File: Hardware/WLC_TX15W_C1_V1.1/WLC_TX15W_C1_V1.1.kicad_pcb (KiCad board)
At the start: 2 copper layers, 57.3 x 42.3 mm, 129 parts, among them J1 Conn_01x05, J2 PWR, Q1 BSZ0910LS, Q2 BSZ0910LS, Q3 BSZ0910LS, Q4 BSS138, Q5 BSZ0910LS, Q6 BSZ0910LS, Q7 BSZ0910LS, Q8 BSS138, Q9 AO3400A, U2 LM358, U3 SLS32AIA020X2USON10XTMA4, U4 WLC1115-68LQXQ, Y2 SG-210STF

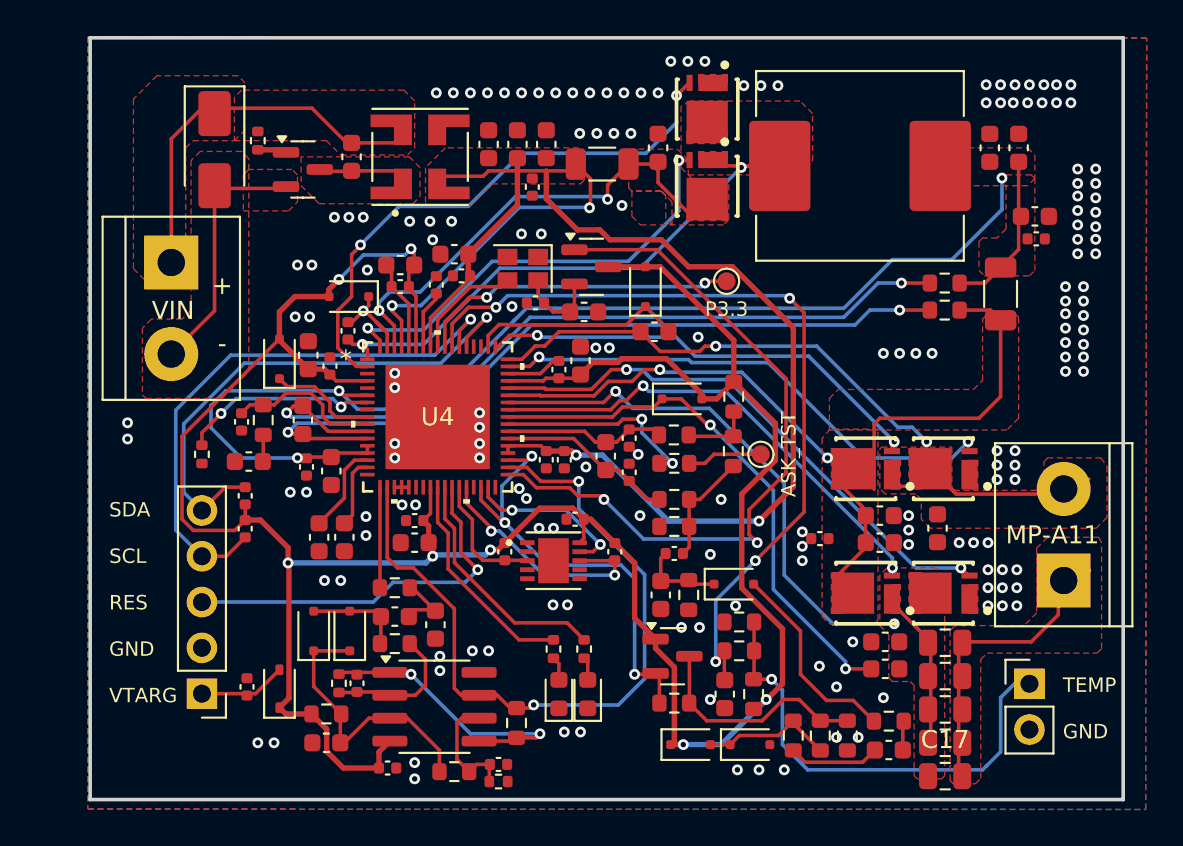
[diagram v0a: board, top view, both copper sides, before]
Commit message: add usb type c
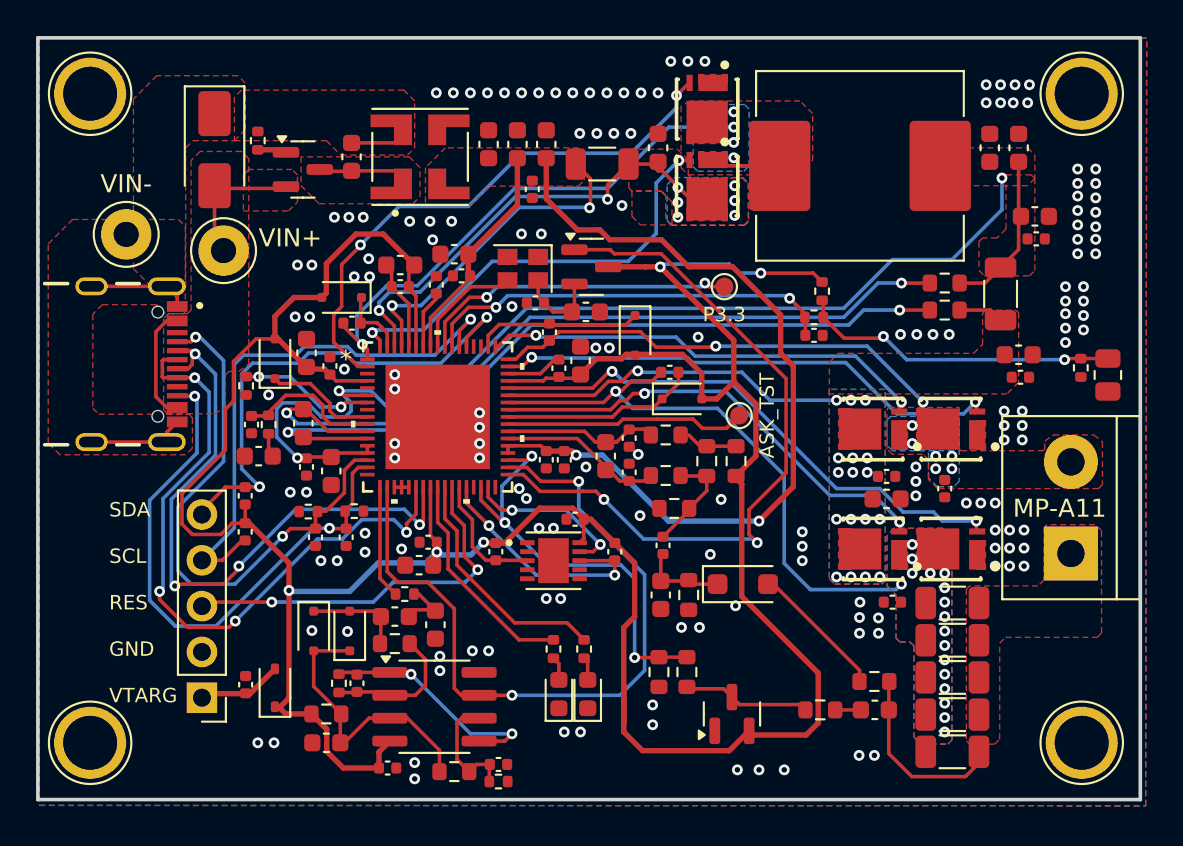
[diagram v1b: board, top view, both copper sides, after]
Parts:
- removed D12, D13: BAT54J, Diode_SMD:D_SOD-323F
- removed J2: PWR, TerminalBlock:TerminalBlock_bornier-2_P5.08mm
- removed Q4: BSS138, Package_TO_SOT_SMD:SOT-23
- removed R33: 0R, Resistor_SMD:R_0603_1608Metric
- added C61: 0.1uF, Capacitor_SMD:C_0402_1005Metric, F.Cu at (156.6, 68.7)
- added D15: MMBD1503, Package_TO_SOT_SMD:SOT-23, F.Cu at (140.6, 87.4)
- added J3: USB4105-GF-A, Footprints-Models:GCT_USB4105-GF-A, F.Cu at (105.1, 68.0)
- added TP3: VIN+, TestPoint:TestPoint_Loop_D3.50mm_Drill1.4mm_Beaded, F.Cu at (112.4, 61.7)
- added TP4: VIN-, TestPoint:TestPoint_Loop_D3.50mm_Drill1.4mm_Beaded, F.Cu at (107.0, 60.8)
- added TP5: GND, TestPoint:TestPoint_Plated_Hole_D3.0mm, F.Cu at (160.0, 53.0)
- added TP6: GND, TestPoint:TestPoint_Plated_Hole_D3.0mm, F.Cu at (105.0, 53.0)
- added TP7: GND, TestPoint:TestPoint_Plated_Hole_D3.0mm, F.Cu at (160.0, 89.0)
- added TP8: GND, TestPoint:TestPoint_Plated_Hole_D3.0mm, F.Cu at (105.0, 89.0)
- C16, C17, C18, C19, C20: footprint Capacitor_SMD:C_0805_2012Metric -> Capacitor_SMD:C_1206_3216Metric
- C2, C23, C24, C25, C26, C31, C32: footprint Capacitor_SMD:C_0603_1608Metric -> Capacitor_SMD:C_0402_1005Metric
- C6: value 100pF -> 150pF
- D10, D4, D5, D6, D7, D9: value BAT54J -> 1PS76SB21
- D11: value BAT54J -> BAS16H; footprint Diode_SMD:D_SOD-323F -> Diode_SMD:D_SOD-123F
- R18, R3, R4, R6, TH1: footprint Resistor_SMD:R_0603_1608Metric -> Resistor_SMD:R_0402_1005Metric
- R22: value 0R -> 5.1K; footprint Resistor_SMD:R_0603_1608Metric -> Resistor_SMD:R_0402_1005Metric
- R9: value 1M -> 5.1K; footprint Resistor_SMD:R_0603_1608Metric -> Resistor_SMD:R_0402_1005Metric
- TH2: footprint Connector_PinHeader_2.54mm:PinHeader_1x02_P2.54mm_Vertical -> Resistor_SMD:R_0805_2012Metric
- moved TH1 23.6 mm to (159.9, 68.2), turned to -90 degrees
- moved R3 22.7 mm to (145.6, 64.0), turned to 90 degrees
- moved C2 20.5 mm to (145.2, 66.4), turned to 180 degrees
- moved R22 20.5 mm to (117.1, 76.2), turned to 0 degrees
- moved C25 20.3 mm to (137.2, 68.5), turned to 0 degrees
- moved R4 19.0 mm to (145.2, 65.4)
- moved TH2 17.7 mm to (161.4, 68.6), turned to -90 degrees
- moved R9 14.8 mm to (119.7, 76.2), turned to 180 degrees
- moved C22 11.8 mm to (156.5, 67.5)
- moved R32 11.0 mm to (136.6, 85.1)
- moved R31 8.20 mm to (138.1, 85.1)
- moved C26 5.83 mm to (130.5, 66.2), turned to 90 degrees
- moved C60 5.06 mm to (149.2, 74.2), turned to 180 degrees
- moved R21 4.52 mm to (113.7, 69.2)
- moved R25 3.58 mm to (140.8, 73.4), turned to 90 degrees
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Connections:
- net CSNO_0 renamed /CSNO_0
- net CSPO_0 renamed /CSPO_0
- net Net-(D8-A1) renamed USB-GND
- net Net-(D8-A2) renamed USB-IN
- C3 pad 2: Net-(D4-K) -> Net-(D4-A)
- C5 pad 1: Net-(D4-A) -> Net-(D4-K)
- D5 pad 1: Net-(D4-K) -> Net-(D4-A)
- D5 pad 2: Net-(D4-A) -> Net-(D4-K)
- R11 pad 2: Net-(D4-K) -> Net-(D4-A)
- R22 pad 1: ASK_TST -> GND
- R22 pad 2: Net-(U4-ASK_TST) -> CC1_0
- R31 pad 2: Net-(Q4-D) -> Q_COMP
- R32 pad 1: Net-(Q4-D) -> Q_COMP
- R5 pad 2: Net-(D4-K) -> Net-(D4-A)
- R7 pad 2: Net-(D4-A) -> Net-(D4-K)
- R9 pad 1: ASK_DEMOD -> GND
- R9 pad 2: Net-(U2B-+) -> CC2_0
- U2 pad 3: Net-(D4-K) -> Net-(D4-A)
- U4 pad 42: Net-(U4-ASK_TST) -> ASK_TST
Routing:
- net D+_0: track 0.00 -> 37.2 mm, vias 0 -> 4
- net D-_0: track 0.00 -> 35.4 mm, vias 0 -> 4
- net CC2_0: track 3.92 -> 31.4 mm, vias 0 -> 2
- net CC1_0: track 5.03 -> 30.5 mm, vias 0 -> 2
- net IOUT_CSN_0: track 44.8 -> 22.0 mm, vias 2 -> 18
- net TEMP_FB1: track 45.6 -> 23.1 mm, vias 4 -> 2
- net VDD: track 152.9 -> 172.4 mm, vias 7 -> 5
- net BST2_1: track 30.3 -> 10.8 mm, vias 2 -> 0
- net SW1_1: track 41.5 -> 25.8 mm, vias 2 -> 8
- net Net-(Q4-D): track 12.8 -> 0.00 mm
- net Net-(U4-ASK_TST): track 11.4 -> 0.00 mm, vias 2 -> 0
- net Net-(D4-K): track 15.7 -> 5.37 mm
- net Net-(D4-A): track 5.37 -> 15.7 mm
- net ASK_TST: track 4.19 -> 13.4 mm
- net Net-(R3-Pad1): track 26.1 -> 17.8 mm, vias 1 -> 2
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- added copper zone on B.Cu, net IIN_CSN_0
- added copper zone on B.Cu, net IOUT_CSN_0
- added copper zone on B.Cu, net SW1_0
- added copper zone on B.Cu, net SW1_1
- added copper zone on B.Cu, net SW2_1
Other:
- board size 57.3 x 42.3 mm -> 61.2 x 42.3 mm
- board text removed: "+ -"
- board text removed: "TEMP GND"
- board text removed: "VIN"

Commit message: update bom
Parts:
- removed TP1: P3.3, TestPoint:TestPoint_Pad_D1.0mm
- removed TP2: ASK_TST, TestPoint:TestPoint_Pad_D1.0mm
- added G***: LOGO, haidv-library:LoGo12mm, B.Cu at (115.6, 55.6)
- C2, C23, C24, C35, C50, C51: footprint Capacitor_SMD:C_0402_1005Metric -> Capacitor_SMD:C_0603_1608Metric
- C3, C33, C4, C5: footprint Capacitor_SMD:C_0603_1608Metric -> Capacitor_SMD:C_0402_1005Metric
- L1: footprint Inductor_SMD:L_Bourns_SRP1050WA -> Inductor_SMD:L_Bourns-SRN8040_8x8.15mm
- R14, R15, R16, R17: footprint Capacitor_SMD:C_0402_1005Metric -> Resistor_SMD:R_0402_1005Metric
- R19, R20, R23, R24, R27, R28, R29, R5, R7: footprint Resistor_SMD:R_0603_1608Metric -> Resistor_SMD:R_0402_1005Metric
- moved R29 6.89 mm to (143.9, 80.4), turned to -90 degrees
- moved D5 5.96 mm to (116.5, 88.0)
- moved C4 5.39 mm to (118.8, 83.4)
- moved D4 5.27 mm to (118.4, 88.0)
- moved R7 4.44 mm to (117.8, 85.3), turned to 90 degrees
- moved C5 4.29 mm to (117.8, 83.4), turned to 90 degrees
- moved C14 3.75 mm to (152.8, 56.0)
- moved C15 3.75 mm to (151.2, 56.0)
- moved R6 3.68 mm to (118.8, 81.5), turned to -90 degrees
- moved C58 3.24 mm to (154.2, 61.4)
- moved C57 3.12 mm to (154.3, 60.1)
- moved D15 2.75 mm to (140.6, 84.7), turned to -90 degrees
- moved D3 2.68 mm to (114.0, 88.3)
- moved C22 2.55 mm to (153.9, 67.5)
- moved C61 2.55 mm to (154.1, 68.8)
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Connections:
- U4 pad 42: ASK_TST -> unconnected-(U4-ASK_TST-Pad42)
- U4 pad 59: P3.3 -> unconnected-(U4-GPIO12-Pad59)
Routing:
- net P3.3: track 17.8 -> 0.00 mm, vias 2 -> 0
- net VDD: track 172.4 -> 154.7 mm
- net ASK_TST: track 13.4 -> 0.00 mm
- net IOUT_CSP_0: track 67.8 -> 58.1 mm
- net COIL_SNS: track 10.5 -> 17.3 mm
- net Net-(D11-A): track 7.68 -> 1.47 mm
- net CC1_0: track 30.5 -> 24.8 mm
- net Net-(D4-A): track 15.7 -> 11.0 mm
- net Net-(U2A--): track 7.79 -> 3.79 mm
- net IIN_CSP_0: track 79.5 -> 76.5 mm
- net Net-(D15-common): track 7.06 -> 5.20 mm
- net CTRL_1: track 40.2 -> 38.5 mm
- net /CSPO_0: track 44.2 -> 42.6 mm
- net /CSNO_0: track 43.0 -> 41.3 mm
- net ASK_DEMOD: track 41.2 -> 39.7 mm
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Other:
- board text added: "WLC_TX15W_C1_V1.1"

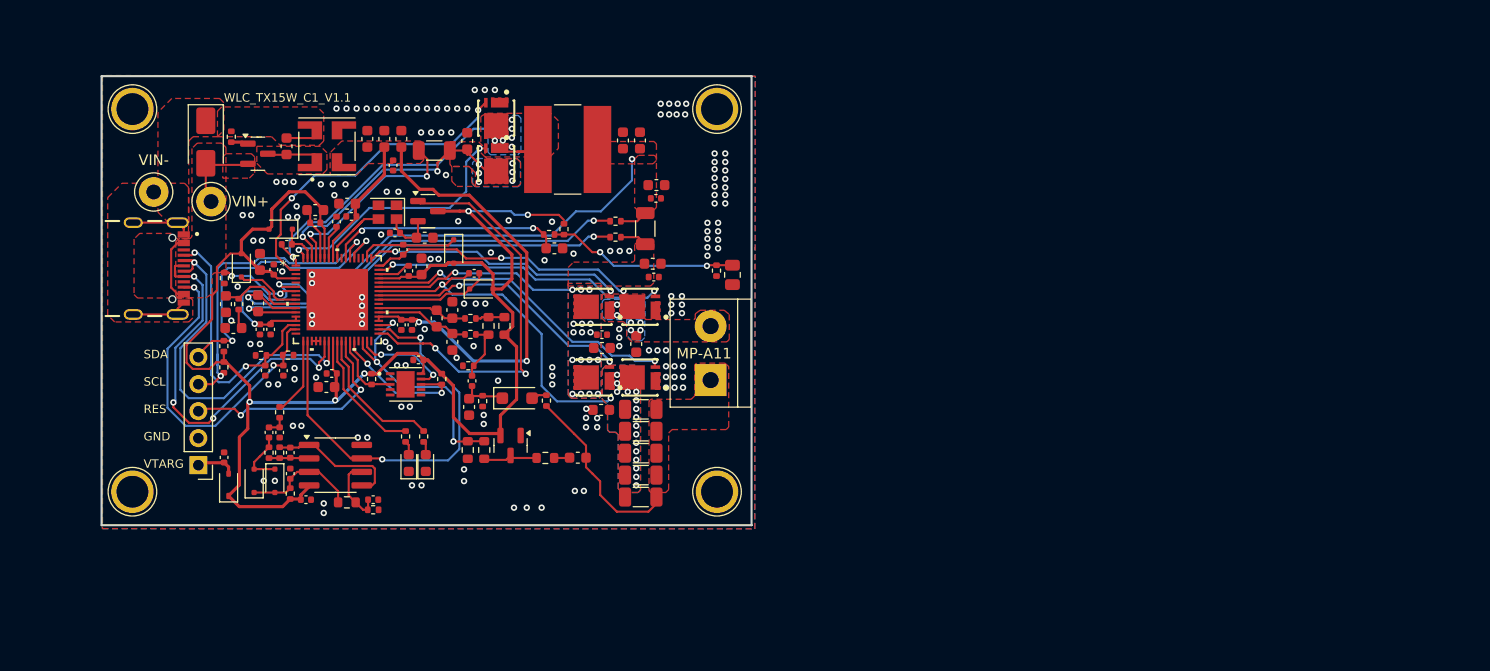
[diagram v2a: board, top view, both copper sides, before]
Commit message: Fix board outline
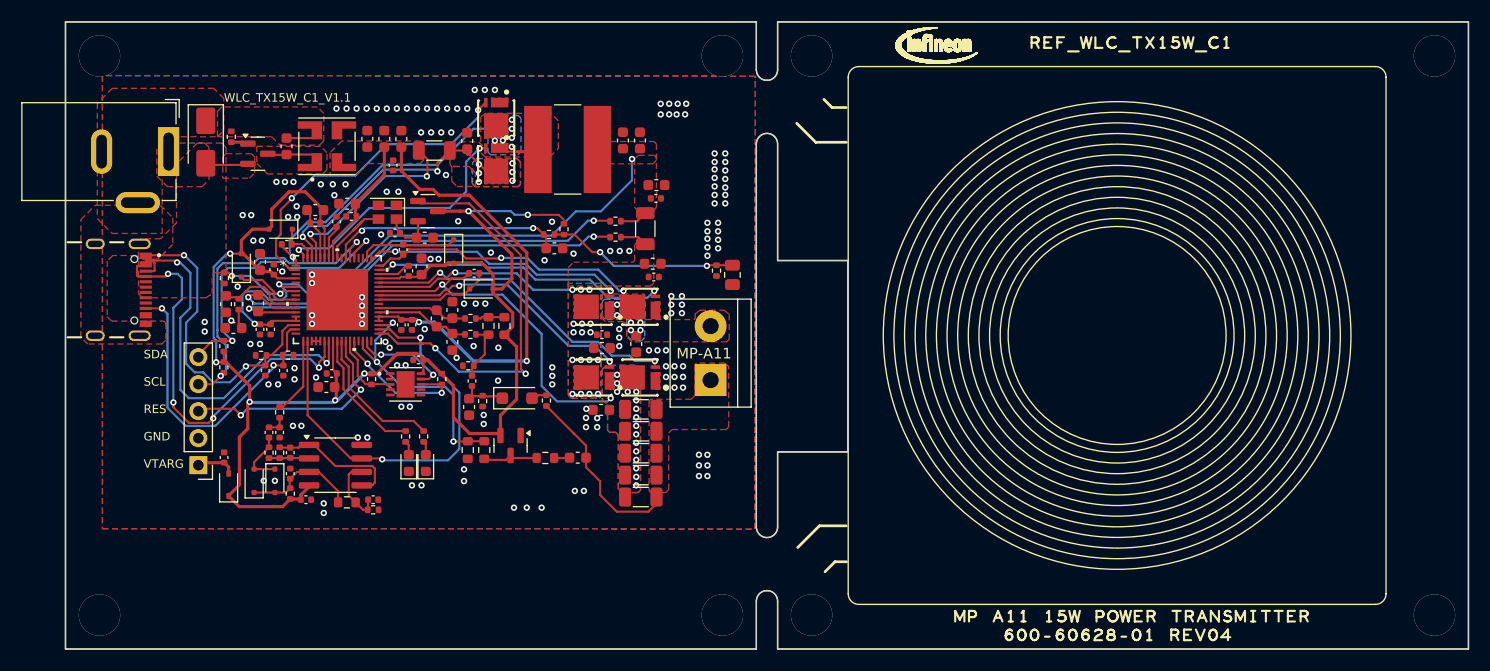
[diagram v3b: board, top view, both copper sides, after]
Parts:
- removed TP3: VIN+, TestPoint:TestPoint_Loop_D3.50mm_Drill1.4mm_Beaded
- removed TP4: VIN-, TestPoint:TestPoint_Loop_D3.50mm_Drill1.4mm_Beaded
- removed TP5, TP6, TP7, TP8: GND, TestPoint:TestPoint_Plated_Hole_D3.0mm
- added J4: Barrel_Jack_Switch, Connector_BarrelJack:BarrelJack_GCT_DCJ200-10-A_Horizontal, F.Cu at (108.4, 57.0)
- moved J3 4.10 mm to (101.5, 70.0)
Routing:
- net USB-GND: track 14.1 -> 3.05 mm
- net USB-IN: track 14.0 -> 3.72 mm
- net CC1_0: track 24.8 -> 29.0 mm
- net VDD: track 154.7 -> 150.6 mm, vias 5 -> 7
- net CC2_0: track 32.0 -> 29.4 mm
- net D-_0: track 34.7 -> 36.8 mm
- net D+_0: track 37.3 -> 38.7 mm
- net HPI_I2C_SCL: track 30.5 -> 29.9 mm
- net GND: vias 161 -> 169
- net (no net): vias 0 -> 8
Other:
- board size 61.2 x 42.3 mm -> 132 x 59 mm
